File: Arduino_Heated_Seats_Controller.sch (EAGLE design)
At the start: 13 parts, among them U1 ULN2003AN, U2 M54564P

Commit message: Initial work on rev3 underway (time for some sleep).
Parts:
- removed BTN, L-TEST: M02PTH, SparkFun-Connectors:M02PTH
- removed L-OUT: (no value), SparkFun-Connectors:M06SIP
- removed PCB1: ARDUINO_NANO, E14_Arduino:ARDUINO_NANO
- removed PWR: (no value), SparkFun-Connectors:M03PTH
- added BTN-IN, LED-TEST: M02PTH, SparkFun-Connectors:M02PTH
- added C1, C4, C5: 0.1uF, rcl:C-USC0603
- added C2: 0.1uF, rcl:CPOL-USCT3216
- added C3: 470pF, rcl:C-USC0603
- added ISP: (no value), con-lstb:MA03-2
- added LED-OUT: (no value), SparkFun-Connectors:M06SIP
- added PWR-LED: (no value), led:LEDCHIP-LED0603
- added PWR/H: (no value), SparkFun-Connectors:M03PTH
- added R5: 10k, resistor:R-US_R0603
- added R6, R7, R8: 1k, resistor:R-US_R0603
- added U3: ULN2003AN, Texas Instruments_By_element14_Batch_1:ULN2003ANE4
- added U4: M54564FP, M54564P-FP:M54564FP
- added XTAL: CSTCE_V, murata-filter:CSTCE_V
- R1, R2, R3, R4: device SparkFun-Resistors:RESISTOR0603-RES -> resistor:R-US_R0603
- U1: value ULN2003AN -> MEGA8-AI; device Texas Instruments_By_element14_Batch_1:ULN2003ANE4 -> atmel:MEGA8-AI
- U2: value M54564P -> (none); device M54564P-FP:M54564P -> v-reg-micrel:MIC5219XX
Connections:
- removed net D10: PCB1.D10, U2.IN8
- removed net D2: BTN-TEST.1, PCB1.D2, R1.1, R3.2
- removed net D3: BTN-TEST.2, PCB1.D3, R2.1, R4.2
- removed net D4: PCB1.D4, U1.7B, U2.IN1
- removed net D5: PCB1.D5, U1.6B, U2.IN2
- removed net D6: PCB1.D6, U1.5B, U2.IN3
- removed net D7: PCB1.D7, U1.3B, U2.IN4
- removed net D8: PCB1.D8, U1.2B, U2.IN5
- removed net D9: PCB1.D9, U1.1B, U2.IN6
- new net ADC0/A0: U1.PC0(ADC0)
- new net ADC1/A1: U1.PC1(ADC1)
- new net ADC2/A2: U1.PC2(ADC2)
- new net ADC3/A3: U1.PC3(ADC3)
- new net ADC4/A4/SDA: U1.PC4(ADC4/SDA)
- new net ADC5/A5/SCL: U1.PC5(ADC5/SCL)
- new net ADC6/A6: U1.ADC6
- new net ADC7/A7: U1.ADC7
- new net AREF: C4.1, U1.AREF
- new net EN: U2.EN
- new net N$3: PWR-LED.A, R8.2
- new net N$4: C3.1, U2.BYP
- new net N$8: R6.1, U1.PD0(RXD)
- new net N$9: R7.1, U1.PD1(TXD)
- new net PB0/D8: U1.PB0(ICP), U3.2B, U4.IN5
- new net PB1/D9: U1.PB1(OC1A), U3.1B, U4.IN6
- new net PB2/D10: U1.PB2(SS/OC1B), U4.IN8
- new net PB3/D11: ISP.4, U1.PB3(MOSI/OC2)
- new net PB4/D12: ISP.1, U1.PB4(MISO)
- new net PB5/D13: ISP.3, U1.PB5(SCK)
- new net PB6: U1.PB6(XTAL1/TOSC1), XTAL.1
- new net PB7: U1.PB7(XTAL2/TOSC2), XTAL.3
- new net PD2/D2: BTN-TEST.1, R1.2, R3.1, U1.PD2(INT0)
- new net PD3/D3: BTN-TEST.2, R2.2, R4.1, U1.PD3(INT1)
- new net PD4/D4: U1.PD4(XCK/T0), U3.7B, U4.IN1
- new net PD5/D5: U1.PD5(T1), U3.6B, U4.IN2
- new net PD6/D6: U1.PD6(AIN0), U3.5B, U4.IN3
- new net PD7/D7: U1.PD7(AIN1), U3.3B, U4.IN4
- new net RESET: ISP.5, R5.2, U1.PC6(/RESET)
- new net RXI: R6.2
- new net TXO: R7.2
- new net VDD: C2.+, C5.1, ISP.2, R5.1, R8.1, U1.AVCC, U1.VCC@1, U1.VCC@2, U2.OUT
- net D-BTN: now also BTN-IN.1, R1.1; no longer BTN.1, R1.2
- net DH-HIGH: now also U4.O1; no longer U2.O1
- net DH-LOW: now also U4.O3; no longer U2.O3
- net DH-MID: now also U4.O2; no longer U2.O2
- net DL-HIGH: now also LED-OUT.1, U3.7C; no longer L-OUT.1, U1.7C
- net DL-LOW: now also LED-OUT.3, U3.5C; no longer L-OUT.3, U1.5C
- net DL-MID: now also LED-OUT.2, U3.6C; no longer L-OUT.2, U1.6C
- net GND: now also C1.2, C2.-, C3.2, C4.2, C5.2, ISP.6, LED-TEST.2, PWR-LED.C, PWR/H.2, R3.2, R4.2, U1.GND@1, U1.GND@2, U3.GND, U4.GND, XTAL.2; no longer L-TEST.2, PCB1.GND, PCB1.GND., PWR.2, R3.1, R4.1
- net H-ON: now also PWR/H.3, U4.O8; no longer PWR.3, U2.O8
- net L-TEST: now also LED-TEST.1, U3.COM; no longer L-TEST.1, U1.COM
- net P-BTN: now also BTN-IN.2, R2.1; no longer BTN.2, R2.2
- net PH-HIGH: now also U4.O4; no longer U2.O4
- net PH-LOW: now also U4.O6; no longer U2.O6
- net PH-MID: now also U4.O5; no longer U2.O5
- net PL-HIGH: now also LED-OUT.4, U3.3C; no longer L-OUT.4, U1.3C
- net PL-LOW: now also LED-OUT.6, U3.1C; no longer L-OUT.6, U1.1C
- net PL-MID: now also LED-OUT.5, U3.2C; no longer L-OUT.5, U1.2C
- net VIN: now also C1.1, PWR/H.1, U2.IN, U4.VS; no longer PCB1.VIN, PWR.1, U2.VS
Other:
- moved on the sheet: BTN-TEST, H-OUT, R1, R2, R3, R4

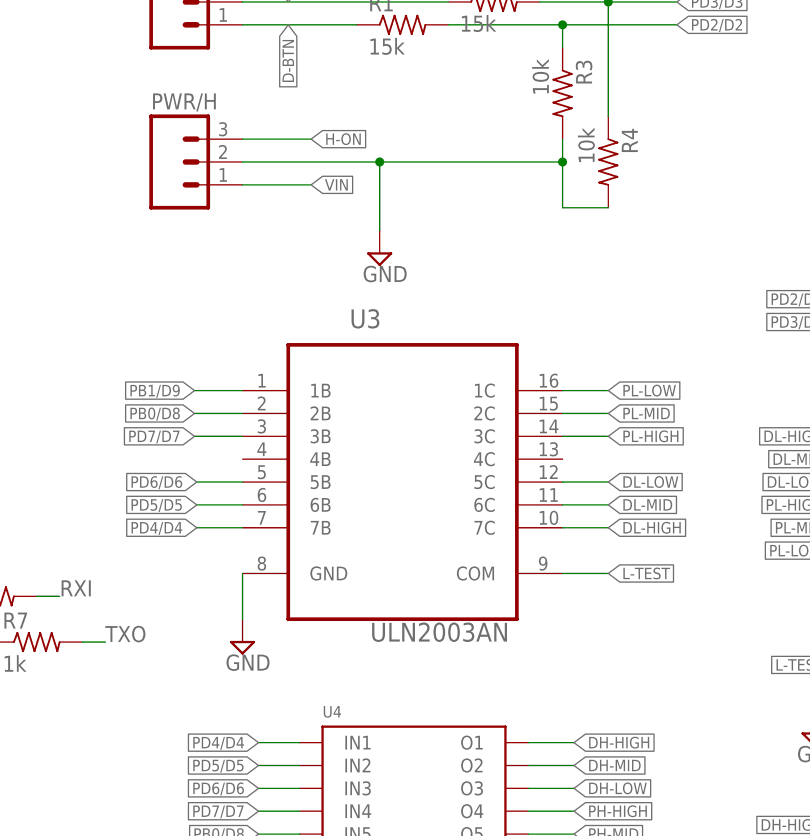
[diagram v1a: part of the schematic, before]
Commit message: ULN2003A replaced with ULN2803A (both from Texas Instruments - but with one more input, cheaper and actually available without jumping to eBay). Work on replacing the M54564P underway.
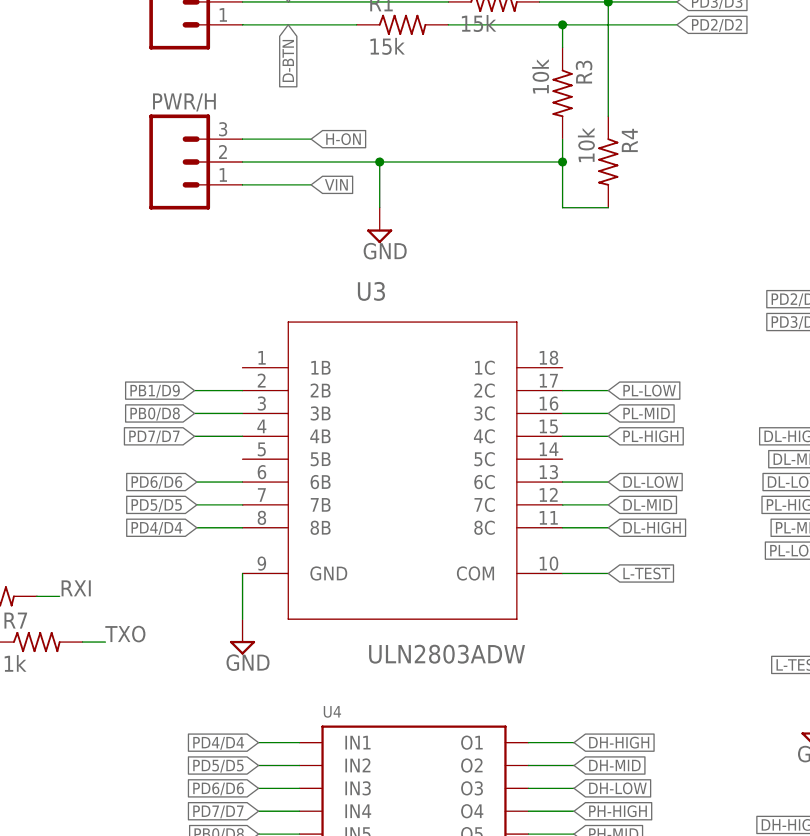
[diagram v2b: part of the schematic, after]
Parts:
- U3: value ULN2003AN -> ULN2803ADW; device Texas Instruments_By_element14_Batch_1:ULN2003ANE4 -> TI-ULN2803ADW:ULN2803ADW
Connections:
- net DL-HIGH: now also U3.8C; no longer U3.7C
- net DL-LOW: now also U3.6C; no longer U3.5C
- net DL-MID: now also U3.7C; no longer U3.6C
- net PB0/D8: now also U3.3B; no longer U3.2B
- net PB1/D9: now also U3.2B; no longer U3.1B
- net PD4/D4: now also U3.8B; no longer U3.7B
- net PD5/D5: now also U3.7B; no longer U3.6B
- net PD6/D6: now also U3.6B; no longer U3.5B
- net PD7/D7: now also U3.4B; no longer U3.3B
- net PL-HIGH: now also U3.4C; no longer U3.3C
- net PL-LOW: now also U3.2C; no longer U3.1C
- net PL-MID: now also U3.3C; no longer U3.2C
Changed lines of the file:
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@@
 <parts>
 <part name="U4" library="M54564P-FP" deviceset="M54564FP" device=""/>
-<part name="U3" library="Texas Instruments_By_element14_Batch_1" deviceset="ULN2003ANE4" device="" value="ULN2003AN"/>
 <part name="BTN-IN" library="SparkFun-Connectors" deviceset="M02" device="PTH" value=""/>
 <part name="PWR/H" library="SparkFun-Connectors" deviceset="M03" device="PTH"/>
@@
 <part name="R3" library="resistor" deviceset="R-US_" device="R0603" value="10k"/>
 <part name="R4" library="resistor" deviceset="R-US_" device="R0603" value="10k"/>
+<part name="U3" library="TI-ULN2803ADW" deviceset="ULN2803ADW" device=""/>
 </parts>
 <sheets>
@@
 <attribute name="MPN" x="158.75" y="43.688" size="1.27" layer="96" display="off"/>
 </instance>
-<instance part="U3" gate="A" x="157.48" y="83.82"/>
 <instance part="BTN-IN" gate="G$1" x="132.08" y="132.08"/>
 <instance part="PWR/H" gate="G$1" x="132.08" y="116.84"/>
@@
 <instance part="SUPPLY11" gate="G$1" x="129.54" y="22.86"/>
 <instance part="SUPPLY16" gate="GND" x="132.08" y="12.7"/>
-<instance part="SUPPLY12" gate="GND" x="154.94" y="106.68"/>
+<instance part="SUPPLY12" gate="GND" x="154.94" y="109.22"/>
 <instance part="SUPPLY17" gate="GND" x="139.7" y="63.5"/>
 <instance part="SUPPLY18" gate="GND" x="160.02" y="22.86"/>
@@
 <instance part="R3" gate="G$1" x="175.26" y="124.46" rot="R270"/>
 <instance part="R4" gate="G$1" x="180.34" y="116.84" rot="R270"/>
+<instance part="U3" gate="A" x="157.48" y="86.36"/>
 </instances>
 <busses>
@@
 <net name="GND" class="0">
 <segment>
-<pinref part="U3" gate="A" pin="GND"/>
 <wire x1="139.7" y1="71.12" x2="139.7" y2="66.04" width="0.1524" layer="91"/>
 <pinref part="SUPPLY17" gate="GND" pin="GND"/>
+<pinref part="U3" gate="A" pin="GND"/>
 </segment>
 <segment>
@@
 </segment>
 <segment>
-<wire x1="154.94" y1="109.22" x2="154.94" y2="116.84" width="0.1524" layer="91"/>
+<wire x1="154.94" y1="111.76" x2="154.94" y2="116.84" width="0.1524" layer="91"/>
 <wire x1="180.34" y1="111.76" x2="175.26" y2="111.76" width="0.1524" layer="91"/>
 <wire x1="175.26" y1="111.76" x2="175.26" y2="116.84" width="0.1524" layer="91"/>
@@
 </segment>
 <segment>
-<pinref part="U3" gate="A" pin="7B"/>
 <wire x1="139.7" y1="76.2" x2="134.62" y2="76.2" width="0.1524" layer="91"/>
 <label x="134.62" y="76.2" size="1.27" layer="95" rot="R180" xref="yes"/>
+<pinref part="U3" gate="A" pin="8B"/>
 </segment>
 <segment>
@@
 </segment>
 <segment>
-<pinref part="U3" gate="A" pin="6B"/>
 <wire x1="139.7" y1="78.74" x2="134.62" y2="78.74" width="0.1524" layer="91"/>
 <label x="134.62" y="78.74" size="1.27" layer="95" rot="R180" xref="yes"/>
+<pinref part="U3" gate="A" pin="7B"/>
 </segment>
 <segment>
@@
 </segment>
 <segment>
-<pinref part="U3" gate="A" pin="3B"/>
 <wire x1="139.7" y1="86.36" x2="134.366" y2="86.36" width="0.1524" layer="91"/>
 <label x="134.366" y="86.36" size="1.27" layer="95" rot="R180" xref="yes"/>
+<pinref part="U3" gate="A" pin="4B"/>
 </segment>
 <segment>
@@
 </segment>
 <segment>
-<pinref part="U3" gate="A" pin="2B"/>
 <wire x1="139.7" y1="88.9" x2="134.366" y2="88.9" width="0.1524" layer="91"/>
 <label x="134.366" y="88.9" size="1.27" layer="95" rot="R180" xref="yes"/>
+<pinref part="U3" gate="A" pin="3B"/>
 </segment>
 <segment>
@@
 </segment>
 <segment>
-<pinref part="U3" gate="A" pin="1B"/>
 <wire x1="139.7" y1="91.44" x2="134.366" y2="91.44" width="0.1524" layer="91"/>
 <label x="134.366" y="91.44" size="1.27" layer="95" rot="R180" xref="yes"/>
+<pinref part="U3" gate="A" pin="2B"/>
 </segment>
 <segment>
@@
 </segment>
 <segment>
-<pinref part="U3" gate="A" pin="7C"/>
 <wire x1="175.26" y1="76.2" x2="180.34" y2="76.2" width="0.1524" layer="91"/>
 <label x="180.34" y="76.2" size="1.27" layer="95" xref="yes"/>
+<pinref part="U3" gate="A" pin="8C"/>
 </segment>
 </net>
@@
 </segment>
 <segment>
-<pinref part="U3" gate="A" pin="6C"/>
 <wire x1="175.26" y1="78.74" x2="180.34" y2="78.74" width="0.1524" layer="91"/>
 <label x="180.34" y="78.74" size="1.27" layer="95" xref="yes"/>
+<pinref part="U3" gate="A" pin="7C"/>
 </segment>
 </net>
@@
 </segment>
 <segment>
-<pinref part="U3" gate="A" pin="5C"/>
 <wire x1="175.26" y1="81.28" x2="180.34" y2="81.28" width="0.1524" layer="91"/>
 <label x="180.34" y="81.28" size="1.27" layer="95" xref="yes"/>
+<pinref part="U3" gate="A" pin="6C"/>
 </segment>
 </net>
@@
 </segment>
 <segment>
-<pinref part="U3" gate="A" pin="3C"/>
 <wire x1="175.26" y1="86.36" x2="180.34" y2="86.36" width="0.1524" layer="91"/>
 <label x="180.34" y="86.36" size="1.27" layer="95" xref="yes"/>
+<pinref part="U3" gate="A" pin="4C"/>
 </segment>
 </net>
@@
 </segment>
 <segment>
-<pinref part="U3" gate="A" pin="2C"/>
 <wire x1="175.26" y1="88.9" x2="180.34" y2="88.9" width="0.1524" layer="91"/>
 <label x="180.34" y="88.9" size="1.27" layer="95" xref="yes"/>
+<pinref part="U3" gate="A" pin="3C"/>
 </segment>
 </net>
@@
 </segment>
 <segment>
-<pinref part="U3" gate="A" pin="1C"/>
 <wire x1="175.26" y1="91.44" x2="180.34" y2="91.44" width="0.1524" layer="91"/>
 <label x="180.34" y="91.44" size="1.27" layer="95" xref="yes"/>
+<pinref part="U3" gate="A" pin="2C"/>
 </segment>
 </net>
 <net name="L-TEST" class="0">
 <segment>
-<pinref part="U3" gate="A" pin="COM"/>
 <wire x1="175.26" y1="71.12" x2="180.34" y2="71.12" width="0.1524" layer="91"/>
 <label x="180.34" y="71.12" size="1.27" layer="95" xref="yes"/>
+<pinref part="U3" gate="A" pin="COM"/>
 </segment>
 <segment>
@@
 </segment>
 <segment>
-<pinref part="U3" gate="A" pin="5B"/>
 <wire x1="139.7" y1="81.28" x2="134.62" y2="81.28" width="0.1524" layer="91"/>
 <label x="134.62" y="81.28" size="1.27" layer="95" rot="R180" xref="yes"/>
-</segment>
-<segment>
+<pinref part="U3" gate="A" pin="6B"/>
+</segment>
+<segment>

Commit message: Revert "ULN2003A replaced with ULN2803A (both from Texas Instruments - but with one more input, cheaper and actually available without jumping to eBay)."
This reverts commit adf95428dccab3bb593bcfff33bcf90c1b5228b2.
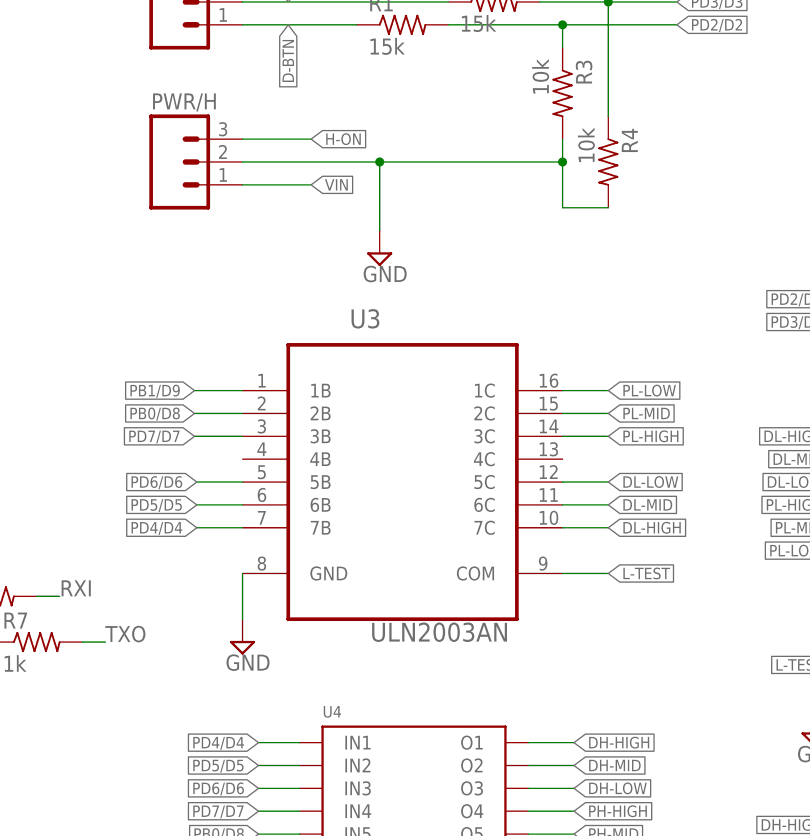
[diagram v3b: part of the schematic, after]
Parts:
- U3: value ULN2803ADW -> ULN2003AN; device TI-ULN2803ADW:ULN2803ADW -> Texas Instruments_By_element14_Batch_1:ULN2003ANE4
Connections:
- net DL-HIGH: now also U3.7C; no longer U3.8C
- net DL-LOW: now also U3.5C; no longer U3.6C
- net DL-MID: now also U3.6C; no longer U3.7C
- net PB0/D8: now also U3.2B; no longer U3.3B
- net PB1/D9: now also U3.1B; no longer U3.2B
- net PD4/D4: now also U3.7B; no longer U3.8B
- net PD5/D5: now also U3.6B; no longer U3.7B
- net PD6/D6: now also U3.5B; no longer U3.6B
- net PD7/D7: now also U3.3B; no longer U3.4B
- net PL-HIGH: now also U3.3C; no longer U3.4C
- net PL-LOW: now also U3.1C; no longer U3.2C
- net PL-MID: now also U3.2C; no longer U3.3C
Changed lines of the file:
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@@
 <parts>
 <part name="U4" library="M54564P-FP" deviceset="M54564FP" device=""/>
+<part name="U3" library="Texas Instruments_By_element14_Batch_1" deviceset="ULN2003ANE4" device="" value="ULN2003AN"/>
 <part name="BTN-IN" library="SparkFun-Connectors" deviceset="M02" device="PTH" value=""/>
 <part name="PWR/H" library="SparkFun-Connectors" deviceset="M03" device="PTH"/>
@@
 <part name="R3" library="resistor" deviceset="R-US_" device="R0603" value="10k"/>
 <part name="R4" library="resistor" deviceset="R-US_" device="R0603" value="10k"/>
-<part name="U3" library="TI-ULN2803ADW" deviceset="ULN2803ADW" device=""/>
 </parts>
 <sheets>
@@
 <attribute name="MPN" x="158.75" y="43.688" size="1.27" layer="96" display="off"/>
 </instance>
+<instance part="U3" gate="A" x="157.48" y="83.82"/>
 <instance part="BTN-IN" gate="G$1" x="132.08" y="132.08"/>
 <instance part="PWR/H" gate="G$1" x="132.08" y="116.84"/>
@@
 <instance part="SUPPLY11" gate="G$1" x="129.54" y="22.86"/>
 <instance part="SUPPLY16" gate="GND" x="132.08" y="12.7"/>
-<instance part="SUPPLY12" gate="GND" x="154.94" y="109.22"/>
+<instance part="SUPPLY12" gate="GND" x="154.94" y="106.68"/>
 <instance part="SUPPLY17" gate="GND" x="139.7" y="63.5"/>
 <instance part="SUPPLY18" gate="GND" x="160.02" y="22.86"/>
@@
 <instance part="R3" gate="G$1" x="175.26" y="124.46" rot="R270"/>
 <instance part="R4" gate="G$1" x="180.34" y="116.84" rot="R270"/>
-<instance part="U3" gate="A" x="157.48" y="86.36"/>
 </instances>
 <busses>
@@
 <net name="GND" class="0">
 <segment>
+<pinref part="U3" gate="A" pin="GND"/>
 <wire x1="139.7" y1="71.12" x2="139.7" y2="66.04" width="0.1524" layer="91"/>
 <pinref part="SUPPLY17" gate="GND" pin="GND"/>
-<pinref part="U3" gate="A" pin="GND"/>
 </segment>
 <segment>
@@
 </segment>
 <segment>
-<wire x1="154.94" y1="111.76" x2="154.94" y2="116.84" width="0.1524" layer="91"/>
+<wire x1="154.94" y1="109.22" x2="154.94" y2="116.84" width="0.1524" layer="91"/>
 <wire x1="180.34" y1="111.76" x2="175.26" y2="111.76" width="0.1524" layer="91"/>
 <wire x1="175.26" y1="111.76" x2="175.26" y2="116.84" width="0.1524" layer="91"/>
@@
 </segment>
 <segment>
+<pinref part="U3" gate="A" pin="7B"/>
 <wire x1="139.7" y1="76.2" x2="134.62" y2="76.2" width="0.1524" layer="91"/>
 <label x="134.62" y="76.2" size="1.27" layer="95" rot="R180" xref="yes"/>
-<pinref part="U3" gate="A" pin="8B"/>
 </segment>
 <segment>
@@
 </segment>
 <segment>
+<pinref part="U3" gate="A" pin="6B"/>
 <wire x1="139.7" y1="78.74" x2="134.62" y2="78.74" width="0.1524" layer="91"/>
 <label x="134.62" y="78.74" size="1.27" layer="95" rot="R180" xref="yes"/>
-<pinref part="U3" gate="A" pin="7B"/>
 </segment>
 <segment>
@@
 </segment>
 <segment>
+<pinref part="U3" gate="A" pin="3B"/>
 <wire x1="139.7" y1="86.36" x2="134.366" y2="86.36" width="0.1524" layer="91"/>
 <label x="134.366" y="86.36" size="1.27" layer="95" rot="R180" xref="yes"/>
-<pinref part="U3" gate="A" pin="4B"/>
 </segment>
 <segment>
@@
 </segment>
 <segment>
+<pinref part="U3" gate="A" pin="2B"/>
 <wire x1="139.7" y1="88.9" x2="134.366" y2="88.9" width="0.1524" layer="91"/>
 <label x="134.366" y="88.9" size="1.27" layer="95" rot="R180" xref="yes"/>
-<pinref part="U3" gate="A" pin="3B"/>
 </segment>
 <segment>
@@
 </segment>
 <segment>
+<pinref part="U3" gate="A" pin="1B"/>
 <wire x1="139.7" y1="91.44" x2="134.366" y2="91.44" width="0.1524" layer="91"/>
 <label x="134.366" y="91.44" size="1.27" layer="95" rot="R180" xref="yes"/>
-<pinref part="U3" gate="A" pin="2B"/>
 </segment>
 <segment>
@@
 </segment>
 <segment>
+<pinref part="U3" gate="A" pin="7C"/>
 <wire x1="175.26" y1="76.2" x2="180.34" y2="76.2" width="0.1524" layer="91"/>
 <label x="180.34" y="76.2" size="1.27" layer="95" xref="yes"/>
-<pinref part="U3" gate="A" pin="8C"/>
 </segment>
 </net>
@@
 </segment>
 <segment>
+<pinref part="U3" gate="A" pin="6C"/>
 <wire x1="175.26" y1="78.74" x2="180.34" y2="78.74" width="0.1524" layer="91"/>
 <label x="180.34" y="78.74" size="1.27" layer="95" xref="yes"/>
-<pinref part="U3" gate="A" pin="7C"/>
 </segment>
 </net>
@@
 </segment>
 <segment>
+<pinref part="U3" gate="A" pin="5C"/>
 <wire x1="175.26" y1="81.28" x2="180.34" y2="81.28" width="0.1524" layer="91"/>
 <label x="180.34" y="81.28" size="1.27" layer="95" xref="yes"/>
-<pinref part="U3" gate="A" pin="6C"/>
 </segment>
 </net>
@@
 </segment>
 <segment>
+<pinref part="U3" gate="A" pin="3C"/>
 <wire x1="175.26" y1="86.36" x2="180.34" y2="86.36" width="0.1524" layer="91"/>
 <label x="180.34" y="86.36" size="1.27" layer="95" xref="yes"/>
-<pinref part="U3" gate="A" pin="4C"/>
 </segment>
 </net>
@@
 </segment>
 <segment>
+<pinref part="U3" gate="A" pin="2C"/>
 <wire x1="175.26" y1="88.9" x2="180.34" y2="88.9" width="0.1524" layer="91"/>
 <label x="180.34" y="88.9" size="1.27" layer="95" xref="yes"/>
-<pinref part="U3" gate="A" pin="3C"/>
 </segment>
 </net>
@@
 </segment>
 <segment>
+<pinref part="U3" gate="A" pin="1C"/>
 <wire x1="175.26" y1="91.44" x2="180.34" y2="91.44" width="0.1524" layer="91"/>
 <label x="180.34" y="91.44" size="1.27" layer="95" xref="yes"/>
-<pinref part="U3" gate="A" pin="2C"/>
 </segment>
 </net>
 <net name="L-TEST" class="0">
 <segment>
+<pinref part="U3" gate="A" pin="COM"/>
 <wire x1="175.26" y1="71.12" x2="180.34" y2="71.12" width="0.1524" layer="91"/>
 <label x="180.34" y="71.12" size="1.27" layer="95" xref="yes"/>
-<pinref part="U3" gate="A" pin="COM"/>
 </segment>
 <segment>
@@
 </segment>
 <segment>
+<pinref part="U3" gate="A" pin="5B"/>
 <wire x1="139.7" y1="81.28" x2="134.62" y2="81.28" width="0.1524" layer="91"/>
 <label x="134.62" y="81.28" size="1.27" layer="95" rot="R180" xref="yes"/>
-<pinref part="U3" gate="A" pin="6B"/>
-</segment>
-<segment>
+</segment>
+<segment>
